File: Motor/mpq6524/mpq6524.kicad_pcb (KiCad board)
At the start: 2 copper layers, 33.6 x 27 mm, 11 parts, among them J1 OQ0212500000G, J2 Conn_02x03_Odd_Even, U1 MPQ6524GRE-AEC1-P, U2 TPS5410DR

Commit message: Paths
Route some paths
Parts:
- moved R2 9.90 mm to (161.8, 70.2), turned to 90 degrees
- moved U1 8.16 mm to (167.6, 71.0)
- moved J2 8.16 mm to (167.6, 80.5)
- moved C2 3.67 mm to (157.4, 84.6)
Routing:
- net +3V3: track 14.0 -> 35.8 mm
- net GND: track 0.00 -> 19.6 mm
- net /fault: track 0.00 -> 11.1 mm
- net +12V: track 17.3 -> 27.8 mm
- net Net-(U2-VSENSE): track 18.1 -> 21.3 mm
- net /MotorEnable: track 13.8 -> 13.0 mm
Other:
- board size 33.6 x 27 mm -> 24.6 x 28.6 mm

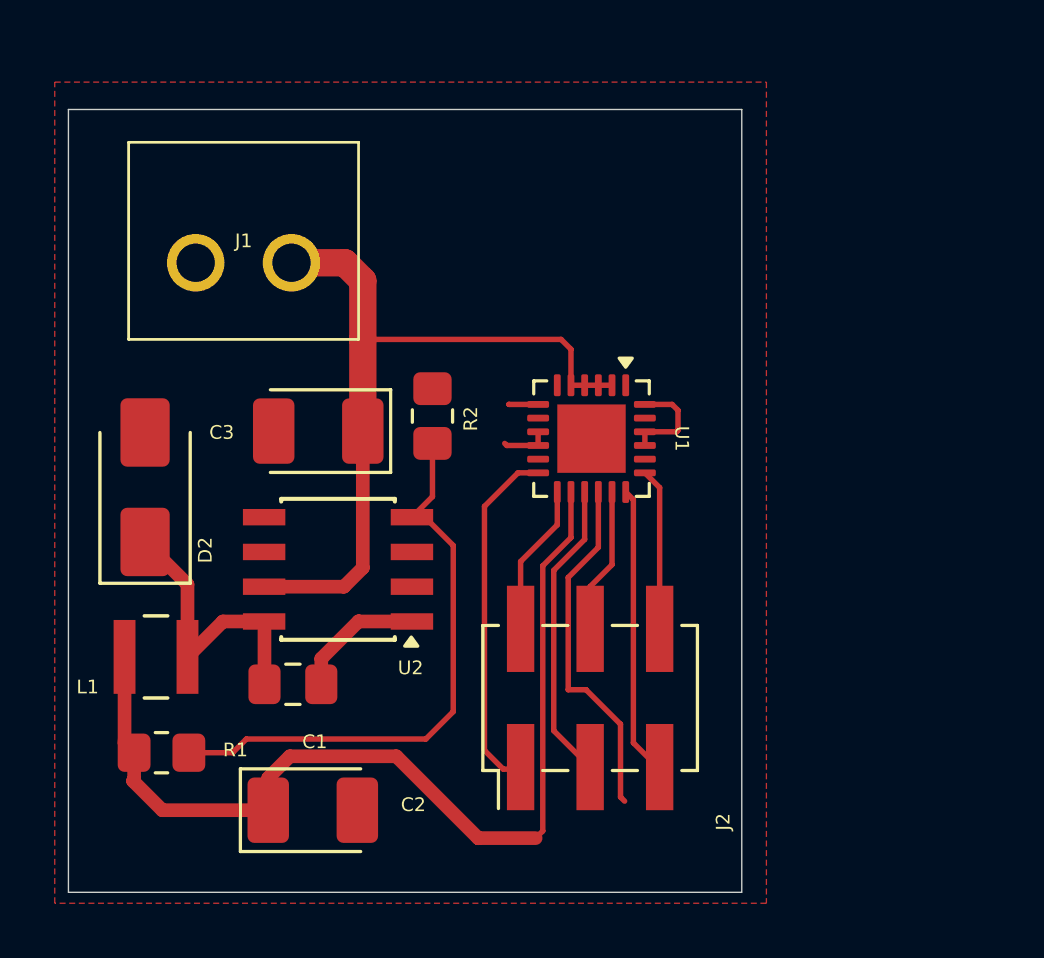
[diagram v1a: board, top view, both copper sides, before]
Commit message: Motor connector
Add motor connector
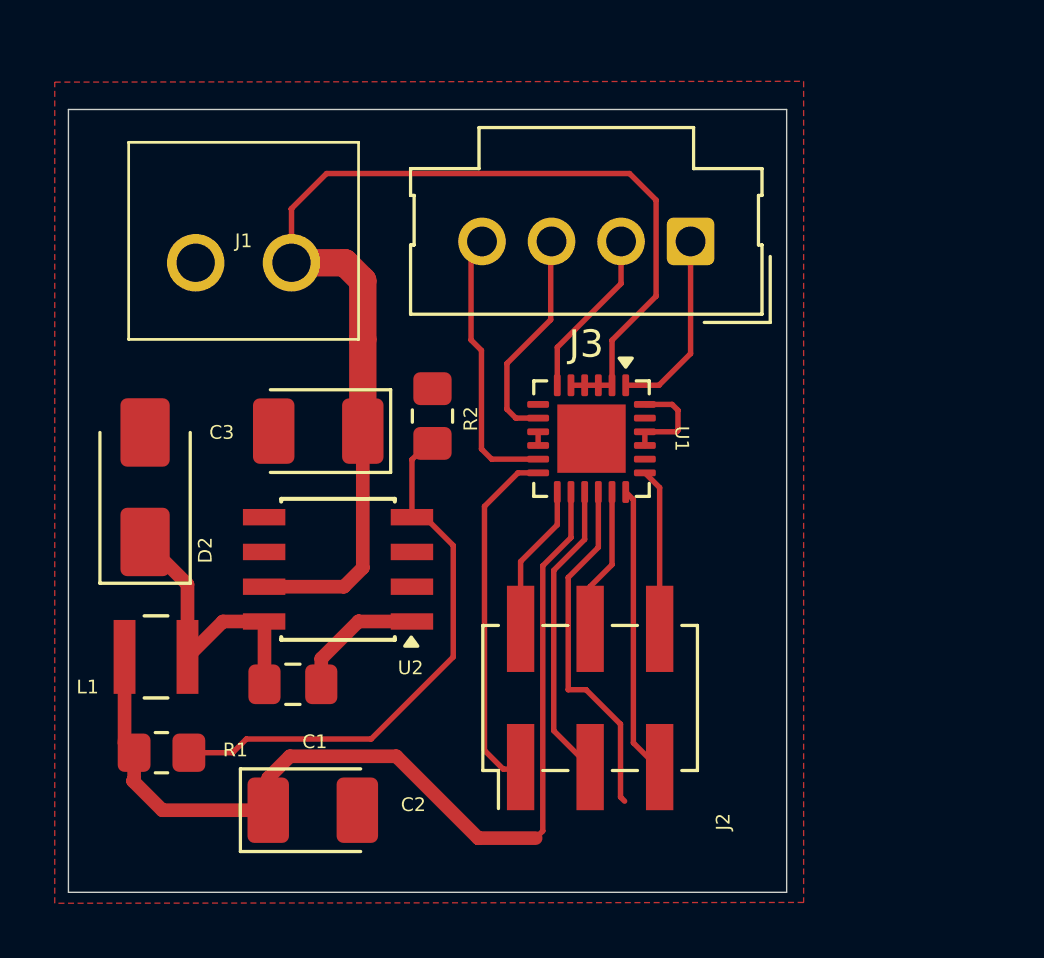
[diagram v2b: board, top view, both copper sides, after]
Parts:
- added J3: Conn_01x04_Socket, Connector_Molex:Molex_SL_171971-0004_1x04_P2.54mm_Vertical, F.Cu at (171.2, 63.8)
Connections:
- U1 pad 1: unconnected-(U1A-OUT4-Pad1) -> /Out4
- U1 pad 11: unconnected-(U1A-OUT1-Pad11) -> /Out1
- U1 pad 12: /MotorEnable -> +3V3
- U1 pad 6: unconnected-(U1A-OUT3-Pad6) -> /Out3
- U1 pad 8: unconnected-(U1A-OUT2-Pad8) -> /Out2
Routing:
- net +12V: track 27.8 -> 42.4 mm
- net /Out1: track 0.00 -> 10.1 mm
- net /Out2: track 0.00 -> 8.08 mm
- net /Out4: track 0.00 -> 6.95 mm
- net /Out3: track 0.00 -> 6.22 mm
- net GND: track 19.6 -> 17.3 mm
- net Net-(U2-VSENSE): track 21.3 -> 20.2 mm
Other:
- board size 24.6 x 28.6 mm -> 26.2 x 28.6 mm

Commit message: Motor connector
added smd connector for the motor outputs
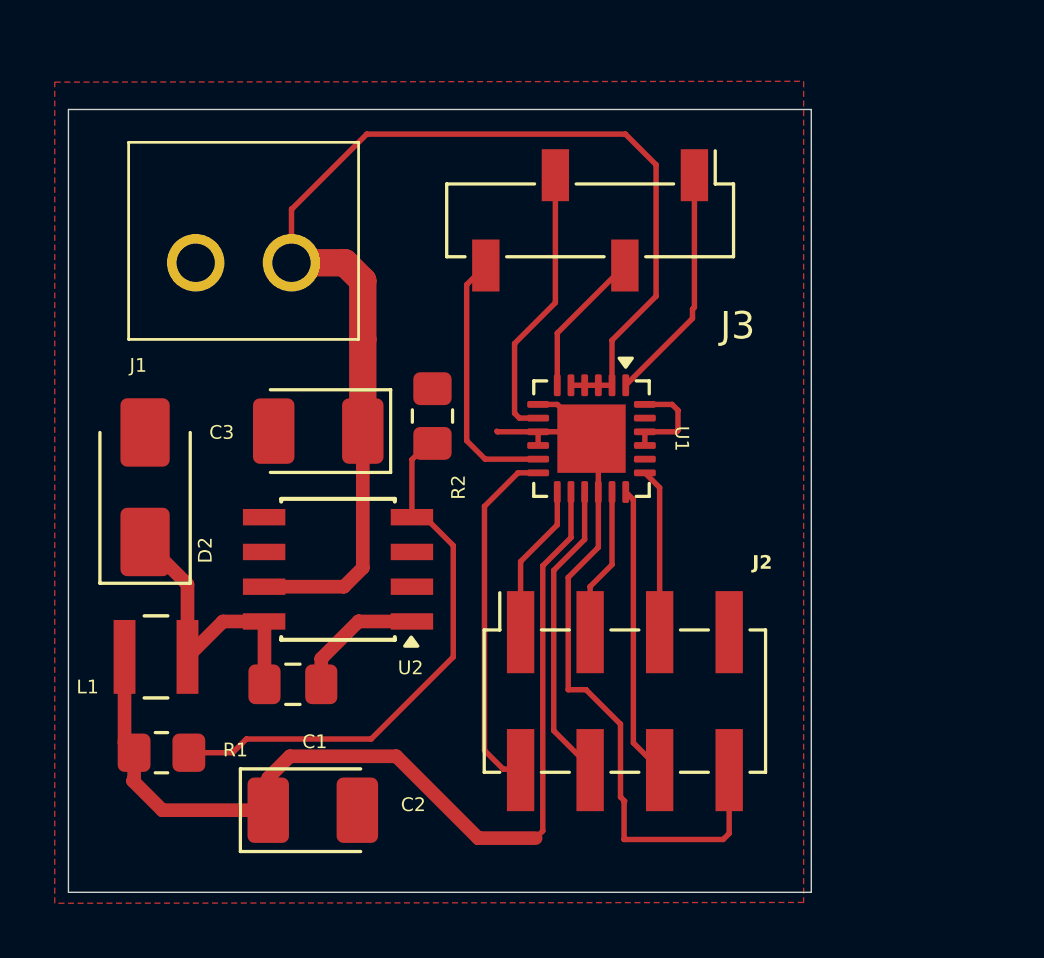
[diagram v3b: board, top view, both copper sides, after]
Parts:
- J2: value Conn_02x03_Odd_Even -> Conn_02x04_Odd_Even; footprint Connector_PinHeader_2.54mm:PinHeader_2x03_P2.54mm_Vertical_SMD -> Connector_PinSocket_2.54mm:PinSocket_2x04_P2.54mm_Vertical_SMD
- J3: value Conn_01x04_Socket -> Conn_01x04; footprint Connector_Molex:Molex_SL_171971-0004_1x04_P2.54mm_Vertical -> Connector_PinSocket_2.54mm:PinSocket_1x04_P2.54mm_Vertical_SMD_Pin1Left
- moved J3 3.75 mm to (167.6, 63.0), turned to -90 degrees
- moved J2 1.28 mm to (168.8, 80.6)
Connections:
- J2 pad 1: /MotorEnable -> /miso
- J2 pad 2: /miso -> /MotorEnable
- J2 pad 3: /fault -> /cs
- J2 pad 4: /cs -> /fault
- J2 pad 5: /clk -> /mosi
- J2 pad 6: /mosi -> /clk
- U1 pad 12: +3V3 -> /MotorEnable
- U1 pad 25: unconnected-(U1B-PAD-Pad25) -> GND
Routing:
- net GND: track 17.3 -> 33.0 mm
- net /Out2: track 8.08 -> 10.2 mm
- net +12V: track 42.4 -> 44.4 mm
- net /Out4: track 6.95 -> 8.71 mm
- net /Out3: track 6.22 -> 5.40 mm
- net /Out1: track 10.1 -> 9.58 mm
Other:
- board size 26.2 x 28.6 mm -> 27.1 x 28.6 mm

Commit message: footprints
Update capacitor footprints
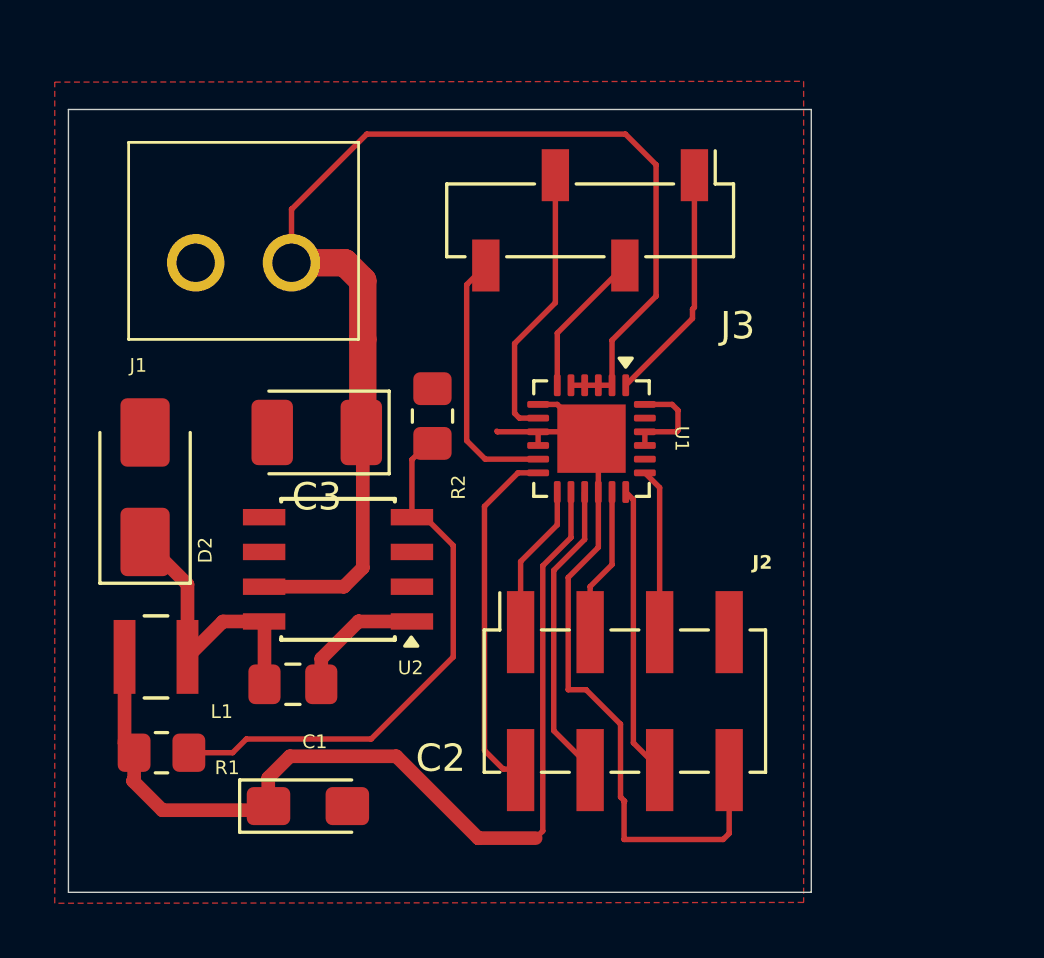
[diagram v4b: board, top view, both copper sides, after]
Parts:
- C2: footprint Capacitor_Tantalum_SMD:CP_EIA-3528-21_Kemet-B_HandSolder -> Capacitor_Tantalum_SMD:CP_EIA-3216-10_Kemet-I_HandSolder
- moved C2 0.23 mm to (157.2, 84.5)
- moved C3 0.07 mm to (157.6, 70.8)

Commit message: traces
Make traces thicker
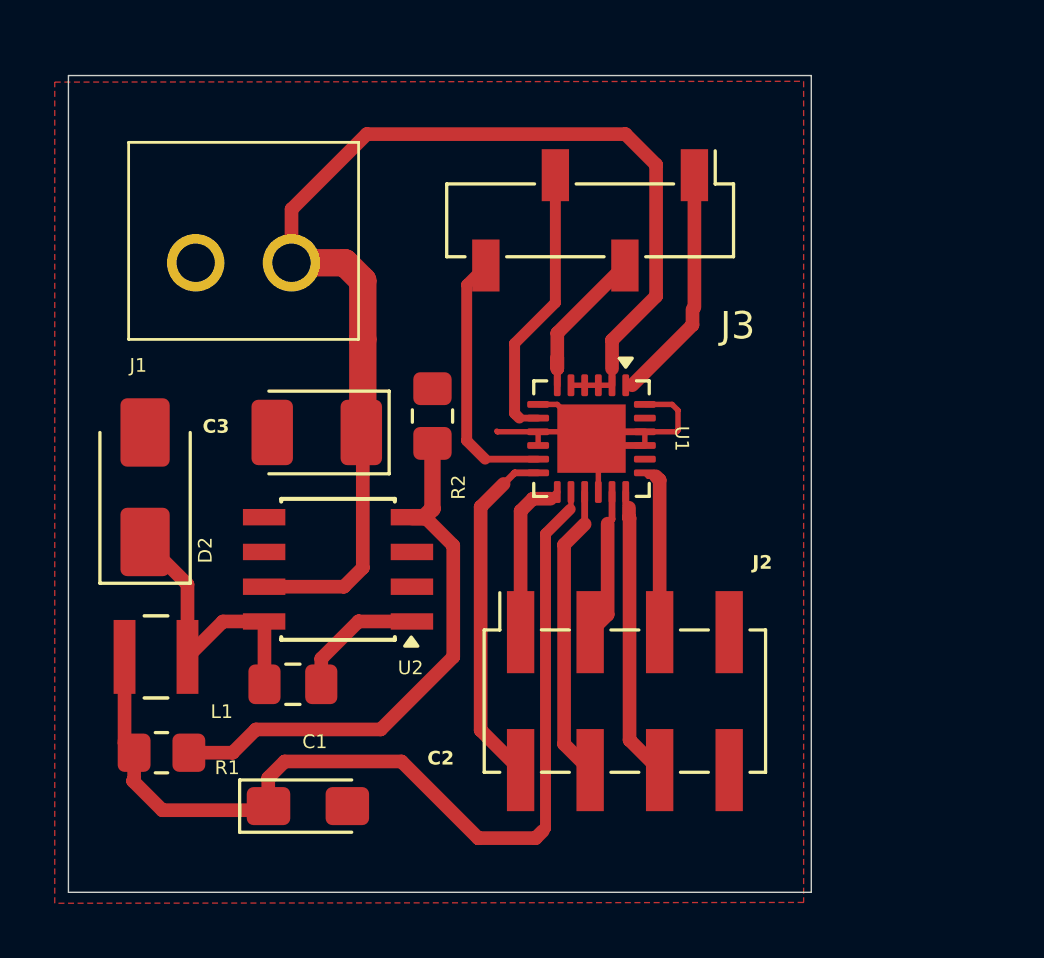
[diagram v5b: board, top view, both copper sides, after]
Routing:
- net GND: track 33.0 -> 16.1 mm
- net /Out3: track 5.40 -> 6.23 mm
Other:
- board size 27.1 x 28.6 mm -> 27.1 x 29.8 mm

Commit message: Layout
Update layouts for the motor drivers
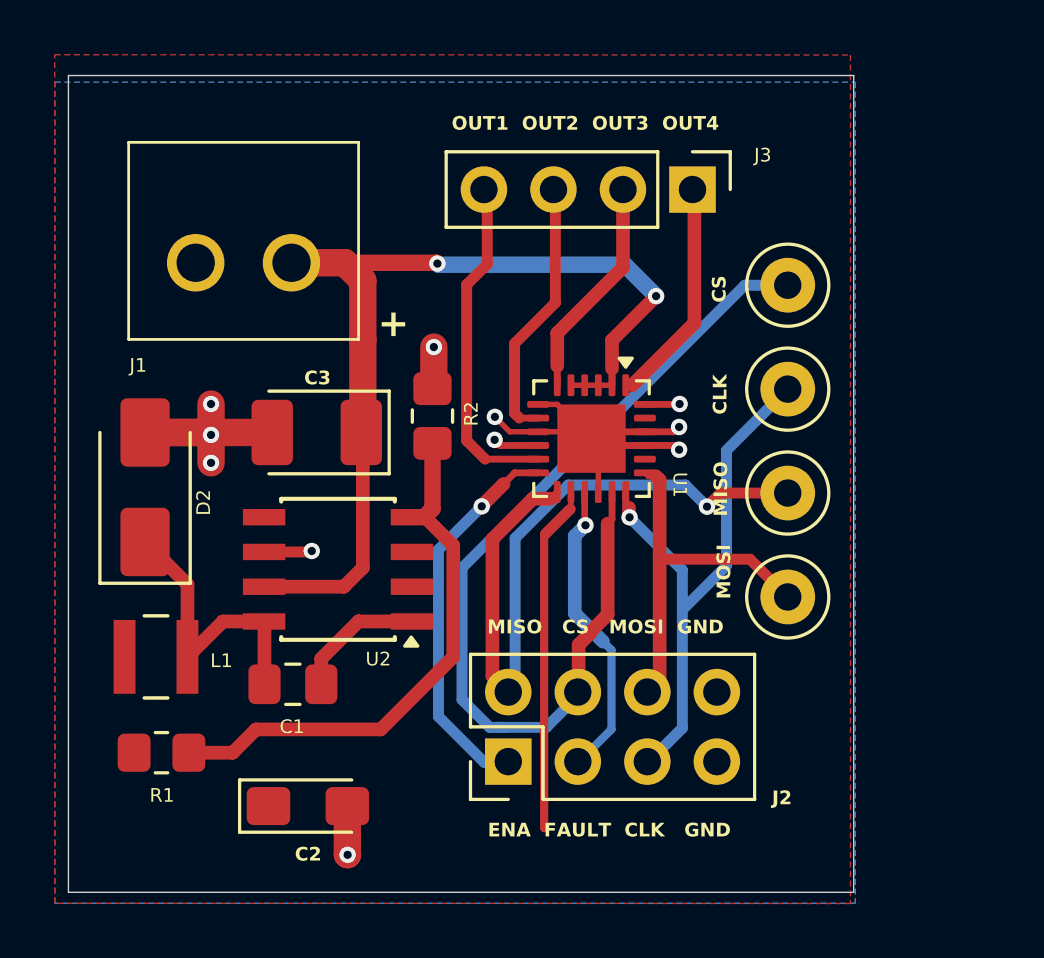
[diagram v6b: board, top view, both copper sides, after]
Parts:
- added TP1: TestPoint, TestPoint:TestPoint_Loop_D1.80mm_Drill1.0mm_Beaded, F.Cu at (174.8, 65.4)
- added TP2: TestPoint, TestPoint:TestPoint_Loop_D1.80mm_Drill1.0mm_Beaded, F.Cu at (174.8, 69.2)
- added TP3: TestPoint, TestPoint:TestPoint_Loop_D1.80mm_Drill1.0mm_Beaded, F.Cu at (174.8, 73.0)
- added TP4: TestPoint, TestPoint:TestPoint_Loop_D1.80mm_Drill1.0mm_Beaded, F.Cu at (174.8, 76.8)
- J2: footprint Connector_PinSocket_2.54mm:PinSocket_2x04_P2.54mm_Vertical_SMD -> Connector_PinHeader_2.54mm:PinHeader_2x04_P2.54mm_Vertical
- J3: footprint Connector_PinSocket_2.54mm:PinSocket_1x04_P2.54mm_Vertical_SMD_Pin1Left -> Connector_PinHeader_2.54mm:PinHeader_1x04_P2.54mm_Vertical
- moved J2 4.80 mm to (164.6, 82.8)
- moved J3 3.91 mm to (171.3, 61.9)
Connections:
- J2 pad 1: /miso -> /MotorEnable
- J2 pad 2: /MotorEnable -> /miso
- J2 pad 3: /cs -> /fault
- J2 pad 4: /fault -> /cs
- J2 pad 5: /mosi -> /clk
- J2 pad 6: /clk -> /mosi
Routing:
- net /cs: track 5.45 -> 34.4 mm
- net +3V3: track 35.6 -> 12.7 mm
- net /miso: track 6.05 -> 25.9 mm, vias 0 -> 1
- net GND: track 16.1 -> 30.9 mm, vias 0 -> 11
- net /clk: track 10.5 -> 20.8 mm, vias 0 -> 1
- net +12V: track 44.4 -> 36.5 mm, vias 0 -> 2
- net /mosi: track 6.16 -> 13.3 mm
- net /Out1: track 9.58 -> 12.3 mm
- net /Out3: track 6.23 -> 8.14 mm
- net /MotorEnable: track 12.8 -> 14.2 mm, vias 0 -> 1
- net Net-(U2-VSENSE): track 20.4 -> 19.5 mm
- net /fault: track 10.9 -> 11.1 mm, vias 0 -> 1
- added copper zone on F.Cu, net +3V3
- added copper zone on B.Cu, net GND
- removed copper zone on F.Cu, net GND
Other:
- board size 27.1 x 29.8 mm -> 28.7 x 29.8 mm
- board text added: "+"
- board text added: "CLK"
- board text added: "CS"
- board text added: "ENA FAULT CLK GND"
- board text added: "MISO"
- board text added: "MISO CS MOSI GND"
- board text added: "MOSI"
- board text added: "OUT1 OUT2 OUT3 OUT4"
